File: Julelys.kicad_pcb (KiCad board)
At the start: 4 copper layers, 65 x 56 mm, 124 parts, among them J1 Raspberry_Pi_40pin, J10 B3B-XH-A, J11 B3B-XH-A, J12 Conn_01x03_Pin, J13 FAN, J3 Conn_02x06_Odd_Even, J4 B3B-XH-A, J5 B3B-XH-A, J6 B3B-XH-A, J7 B3B-XH-A, J8 B3B-XH-A, J9 B3B-XH-A, P1 USB_C_Receptacle_USB2.0, Q1 AO3400A, SW1 SW_Push, SW2 SW_Push, U1 ESP32-C3-WROOM-02, U10 74LVC1G08, U2 74HC4051, U3 AMS1117-3.3, U4 BC847BDW1T1G, U5 CP2102N-A02-GQFN28, U6 74AHCT1G125, U7 74AHCT1G125, U8 74AHCT1G125, U9 74AHCT1G125

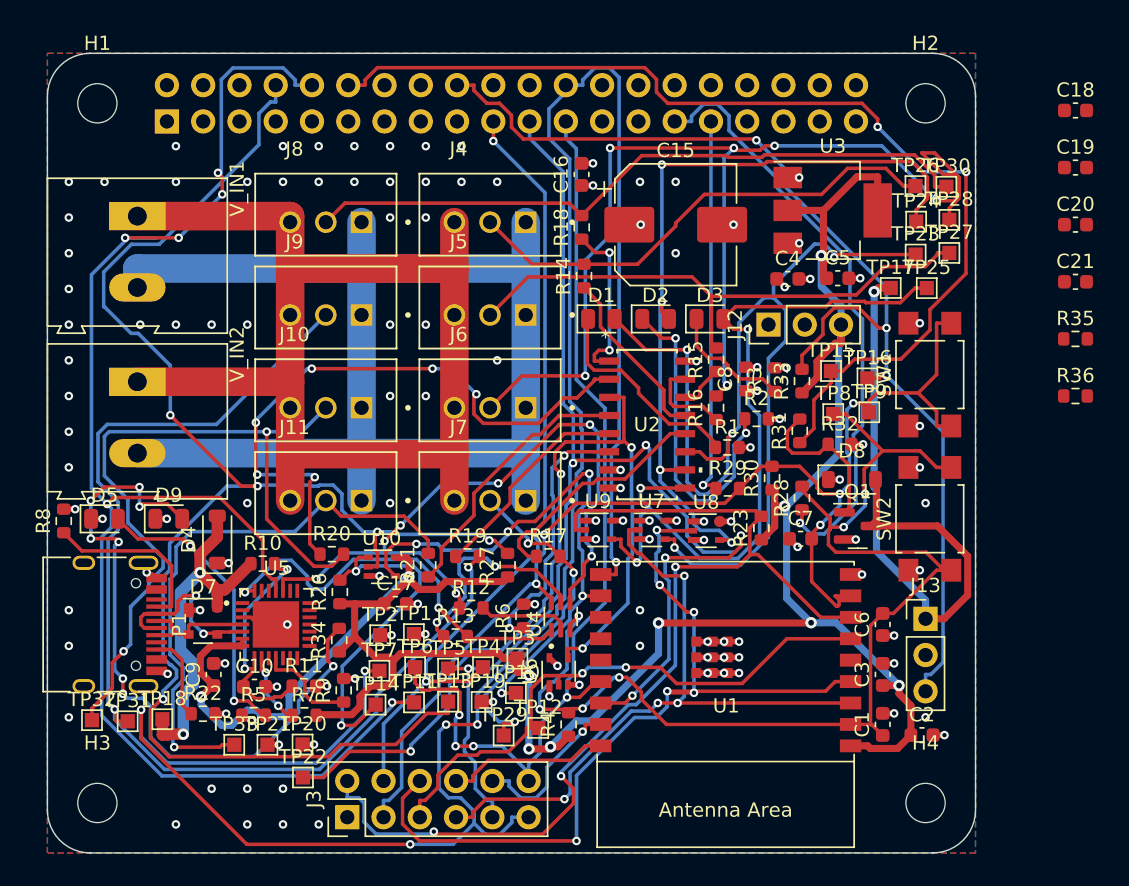
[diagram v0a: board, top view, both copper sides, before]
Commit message: Place decoupling caps, remove fan circuit and J3, add spare ESP32-Pi lines
Schematic:
- Remove the fan circuit (J13, Q1, D8, R31-R33, TP15-17); the Pi 5 drives
  its own Active Cooler. J1 pins 12/18 are now no-connect
- Remove the J3 debug header; J1 doubles as the dev header without a Pi
- IO0/IO1 to J1 pins 37/36 (Pi GPIO26/16) through R37/R38 1k as spare lines

Board:
- Test points moved to the bottom side to free space on top
- Decoupling caps C2/C3/C5/C8/C16/C18-C21 and R35/R36 placed next to
  their ICs; U8 nudged and R23/R10 moved to make room
- Conflicting tracks ripped up and rerouted; 6 connections left for
  interactive routing
- Back pinout table updated (fan and J3 rows replaced by J1 37/36)
- Courtyard exception rule for caps inside their IC's courtyard margin
- DRC (JLCPCB rules): 0 errors; ERC: 0 errors; schematic parity clean

Co-Authored-By: Claude Opus 5.5 <noreply@anthropic.com>
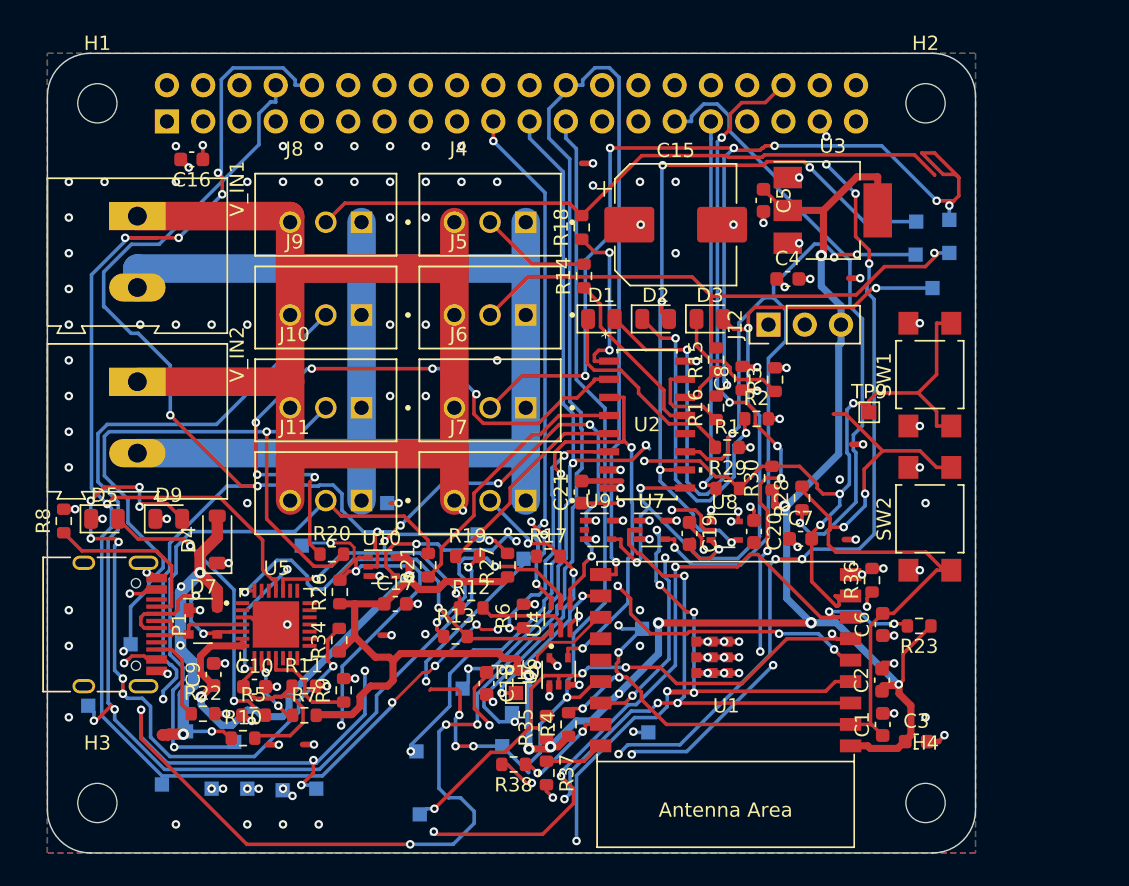
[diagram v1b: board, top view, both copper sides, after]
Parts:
- removed D8: 1N5819HW-7-F, Diode_SMD:D_SOD-123
- removed J13: FAN, Connector_PinHeader_2.54mm:PinHeader_1x03_P2.54mm_Vertical
- removed J3: Conn_02x06_Odd_Even, Connector_PinHeader_2.54mm:PinHeader_2x06_P2.54mm_Vertical
- removed Q1: AO3400A, Package_TO_SOT_SMD:SOT-23
- removed R31: 100, Resistor_SMD:R_0603_1608Metric
- removed R32: 100K, Resistor_SMD:R_0603_1608Metric
- removed R33: 10K, Resistor_SMD:R_0603_1608Metric
- removed TP15: FAN_PWM, TestPoint:TestPoint_Pad_1.0x1.0mm
- removed TP16: FAN_TACH, TestPoint:TestPoint_Pad_1.0x1.0mm
- removed TP17: FAN_N, TestPoint:TestPoint_Pad_1.0x1.0mm
- added R37: 1K, R_0603_1608Metric, F.Cu at (55.0, 62.4)
- added R38: 1K, R_0603_1608Metric, F.Cu at (52.6, 61.8)
- TP1, TP11, TP12, TP13, TP14, TP18, TP19, TP2, TP20, TP21, TP22, TP23, TP24, TP25, TP26, TP27, TP28, TP29, TP3, TP30, TP31, TP32, TP33, TP4, TP5, TP6, TP7, TP8: moved to B.Cu
- moved C18 57.5 mm to (50.8, 56.1), turned to -90 degrees
- moved R35 46.0 mm to (55.0, 59.2), turned to 90 degrees
- moved TP30 43.5 mm to (39.5, 23.8), turned to 180 degrees
- moved C21 37.6 mm to (57.4, 42.7), turned to 90 degrees
- moved C19 37.2 mm to (65.0, 45.6), turned to -90 degrees
- moved C20 31.1 mm to (69.5, 45.5), turned to -90 degrees
- moved TP26 29.9 mm to (51.0, 23.8), turned to 180 degrees
- moved C16 27.3 mm to (30.1, 19.4), turned to 180 degrees
- moved TP8 20.1 mm to (61.6, 52.3), turned to 180 degrees
- moved R36 19.2 mm to (77.8, 48.9), turned to 90 degrees
- moved TP11 18.6 mm to (28.0, 63.2), turned to 180 degrees
- moved TP19 15.2 mm to (36.5, 63.6), turned to 180 degrees
- moved R23 13.0 mm to (81.0, 52.1), turned to 180 degrees
- moved R10 12.3 mm to (33.7, 60.0)
- moved TP14 12.3 mm to (37.8, 46.5), turned to 180 degrees
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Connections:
- J1 pad 12: FAN_PWM -> unconnected-(J1-Pin_12-Pad12)
- J1 pad 18: FAN_TACH -> unconnected-(J1-Pin_18-Pad18)
- J1 pad 36: unconnected-(J1-Pin_36-Pad36) -> PI_GPIO16
- J1 pad 37: unconnected-(J1-Pin_37-Pad37) -> PI_GPIO26
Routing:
- net FAN_TACH: track 78.9 -> 0.00 mm, vias 3 -> 0
- net FAN_PWM: track 74.0 -> 0.00 mm, vias 2 -> 0
- net PI_GPIO16: track 0.00 -> 71.5 mm, vias 0 -> 9
- net PI_GPIO26: track 0.00 -> 65.5 mm, vias 0 -> 8
- net /Power/FAN_N: track 43.1 -> 0.00 mm, vias 1 -> 0
- net IO2: track 94.6 -> 64.5 mm, vias 6 -> 5
- net /CH1: track 34.4 -> 7.80 mm
- net PI_TX: track 109.7 -> 83.2 mm
- net A2: track 72.9 -> 53.6 mm, vias 3 -> 5
- net TXD: track 105.8 -> 124.0 mm, vias 6 -> 10
- net IO9: track 84.6 -> 66.8 mm, vias 5 -> 7
- net /MCH4: track 16.7 -> 0.00 mm
- net GND: track 147.3 -> 163.6 mm, vias 115 -> 121
- net IO6: track 56.9 -> 72.8 mm, vias 2 -> 6
- net VBUS: track 25.6 -> 38.4 mm, vias 2 -> 7
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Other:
- board text added: "IO0 / IO1 (1k)"
- board text added: "J1 37/36"
- board text removed: "1 FAN- 2 +5V 3 TACH"
- board text removed: "1 GND 2 IO8 3 IO9"
- board text removed: "10 IO1 11 IO10 12 IO3"
- board text removed: "4 IO6 5 IO7 6 IO5"
- board text removed: "7 IO4 8 IO0 9 IO2"
- board text removed: "J13 FAN"
- board text removed: "J3"

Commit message: Re-layout v4 with ESP32 under the GPIO header, board fully routed
- ESP32 (U1) top-right under J1, antenna at the right edge (used only as a
  standalone dev board; on the Pi the link is SPI). Short SPI/UART/EN/BOOT
  and spare lines to J1
- Mux U2 with level shifters, series resistors and D1-D3 bottom-centre;
  regulator U3 and Pi bulk cap C15 bottom-left next to the CP2102N
- All decoupling caps 1.7-3.2 mm from their IC pins (C16 5 mm from J1)
- R5 moved next to D5 to free the U5 pin escape; buttons moved under
  the antenna area on the right edge
- Routed with Freerouting plus scripted cleanup; keep-outs now read from
  the board's rule areas
- DRC (JLCPCB rules): 0 errors, 0 unconnected; ERC 0 errors; parity clean

Co-Authored-By: Claude Opus 5.5 <noreply@anthropic.com>
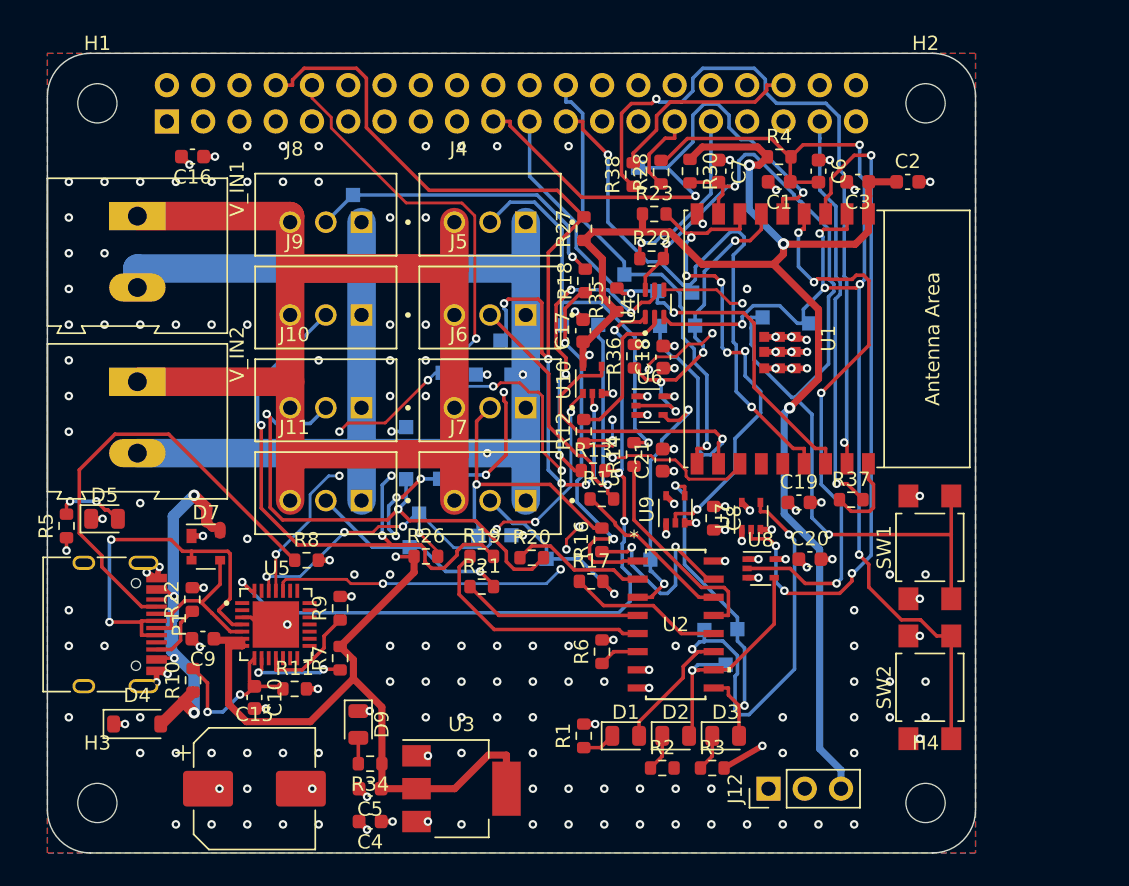
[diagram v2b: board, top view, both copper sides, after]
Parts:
- TP10, TP9: moved to B.Cu
- moved C5 49.6 mm to (42.6, 63.5), turned to 180 degrees
- moved C15 49.3 mm to (34.5, 63.5)
- moved U3 48.1 mm to (49.0, 63.5)
- moved C4 48.0 mm to (42.6, 65.8), turned to 180 degrees
- moved R4 42.4 mm to (71.2, 19.2), turned to 0 degrees
- moved R38 42.2 mm to (61.0, 20.5), turned to 90 degrees
- moved TP7 42.0 mm to (60.4, 27.5)
- moved TP28 39.7 mm to (50.2, 45.8)
- moved C3 39.4 mm to (76.8, 21.0), turned to 180 degrees
- moved TP12 39.3 mm to (65.4, 31.1)
- moved C1 38.7 mm to (71.2, 21.0), turned to 180 degrees
- moved C2 34.9 mm to (80.2, 21.0), turned to 0 degrees
- moved TP11 34.9 mm to (47.7, 34.4)
- moved TP6 34.4 mm to (65.2, 28.8)
- moved R23 34.3 mm to (62.5, 23.2), turned to 0 degrees
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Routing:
- net CS: track 156.8 -> 32.9 mm, vias 8 -> 1
- net /CH3: track 78.0 -> 19.6 mm, vias 7 -> 1
- net PI_GPIO16: track 71.5 -> 14.0 mm, vias 9 -> 0
- net /Power/LED_3V3: track 48.4 -> 1.81 mm, vias 8 -> 0
- net TXD: track 124.0 -> 78.5 mm, vias 10 -> 8
- net IO1: track 7.12 -> 49.3 mm
- net /AS0: track 77.3 -> 36.2 mm, vias 5 -> 2
- net PI_GPIO26: track 65.5 -> 28.5 mm, vias 8 -> 1
- net PI_EN: track 42.3 -> 5.85 mm, vias 1 -> 0
- net /Data: track 53.8 -> 18.4 mm, vias 4 -> 2
- net /AS1: track 52.7 -> 17.5 mm, vias 5 -> 1
- net /MCH7: track 44.0 -> 9.55 mm, vias 6 -> 0
- net IO6: track 72.8 -> 39.7 mm, vias 6 -> 2
- net /CH6: track 80.0 -> 47.0 mm, vias 3 -> 4
- net /AS2: track 53.4 -> 23.8 mm, vias 4 -> 2
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
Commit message: Test board layout: bare ESP32-C3 placed and mostly routed (WIP)
- Board synced to the new schematic: CP2102N/U4/U10 removed; ESP32-C3FH4,
  crystal, RF match, Walsin antenna, TVS, pull-downs and new caps added
- Project footprint library Julelys.pretty with the Walsin RFANT3216120A5T
  land pattern and a 6x6 mm antenna keep-out (no pour, feed track allowed)
- Stackup set to JLC04161H-7628 (0.21 mm prepreg); RF (0.33 mm) and USB
  net classes; In2.Cu is a mixed layer (signals + +5V pour)
- Zones join SMD pads solid; J1 solid to the planes
- DRC: 0 errors; 14 QFN fan-out connections left for interactive routing
  (listed in docs/esp32-c3-chip-design.md)

Co-Authored-By: Claude Opus 5.5 <noreply@anthropic.com>
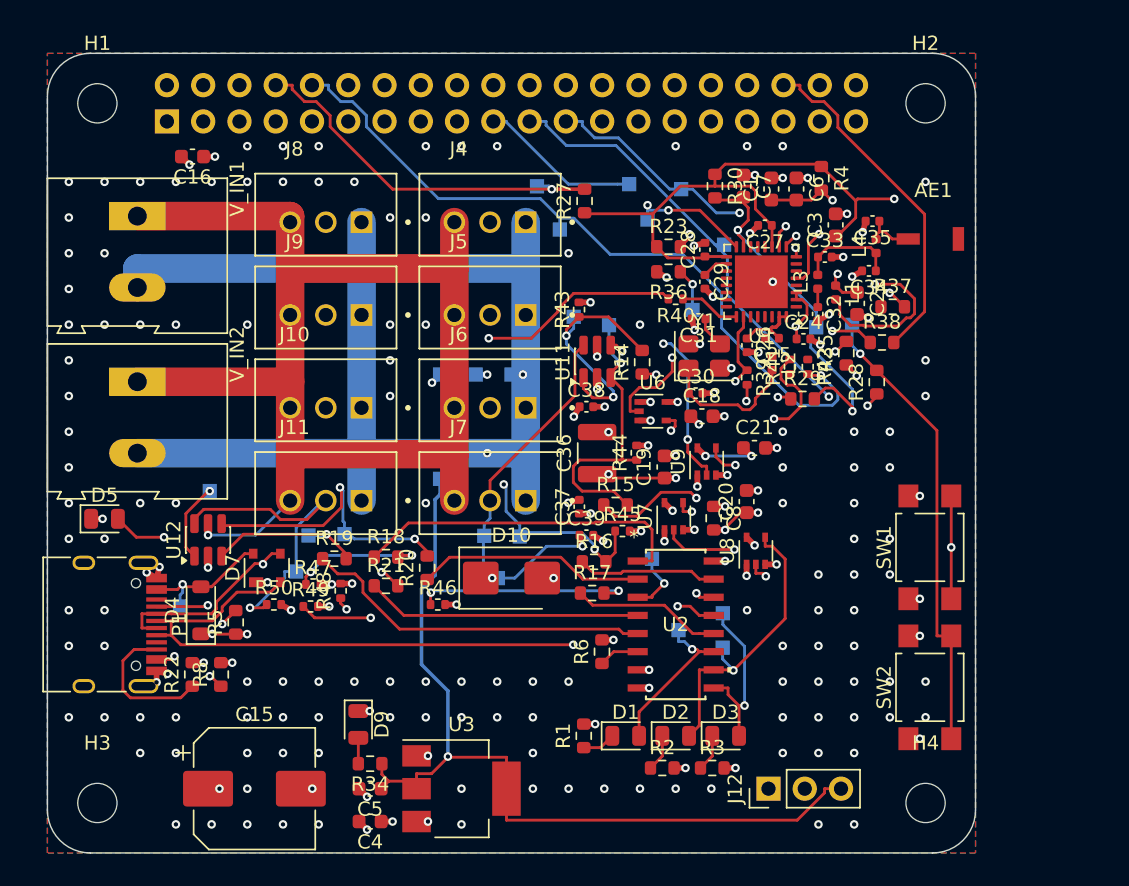
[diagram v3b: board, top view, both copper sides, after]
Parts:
- removed C10: 1uF/16V(10%), Capacitor_SMD:C_0603_1608Metric
- removed C17: 100nF, Capacitor_SMD:C_0603_1608Metric
- removed C9: 10uF/25V(20%), Capacitor_SMD:C_0603_1608Metric
- removed R10: 22.1K, Resistor_SMD:R_0603_1608Metric
- removed R11: 47.5K, Resistor_SMD:R_0603_1608Metric
- removed R12, R13: 10k, Resistor_SMD:R_0603_1608Metric
- removed R26, R9: 10K, Resistor_SMD:R_0603_1608Metric
- removed R7: 1K, Resistor_SMD:R_0603_1608Metric
- removed TP13: PI_TX, TestPoint:TestPoint_Pad_1.0x1.0mm
- removed TP14: USB_TX, TestPoint:TestPoint_Pad_1.0x1.0mm
- removed U10: 74LVC1G08, Package_TO_SOT_SMD:SOT-353_SC-70-5
- removed U4: BC847BDW1T1G, Transistor_Power_Module:SOT65P210X110-6N
- removed U5: CP2102N-A02-GQFN28, Connector_USB:QFN50P500X500X80-29N
- added AE1: RFANT3216120A5T, Julelys:Walsin_RFANT3216120A5T, F.Cu at (80.3, 25.0)
- added C24: 1uF, Capacitor_SMD:C_0402_1005Metric, F.Cu at (73.0, 32.0)
- added C25: 1uF, Capacitor_SMD:C_0402_1005Metric, F.Cu at (70.8, 31.9)
- added C26: 10nF, Capacitor_SMD:C_0402_1005Metric, F.Cu at (69.0, 32.5)
- added C27: 100nF, Capacitor_SMD:C_0402_1005Metric, F.Cu at (70.2, 24.1)
- added C28: 100nF, Capacitor_SMD:C_0402_1005Metric, F.Cu at (66.0, 25.8)
- added C29: 1uF, Capacitor_SMD:C_0402_1005Metric, F.Cu at (66.0, 28.0)
- added C30: 22pF, Capacitor_SMD:C_0402_1005Metric, F.Cu at (65.4, 35.8)
- added C31: 22pF, Capacitor_SMD:C_0402_1005Metric, F.Cu at (65.6, 30.6)
- added C32: 1.5pF, Capacitor_SMD:C_0402_1005Metric, F.Cu at (74.0, 30.2)
- added C33: 1.5pF, Capacitor_SMD:C_0402_1005Metric, F.Cu at (74.5, 26.3)
- added C34: DNP, Capacitor_SMD:C_0402_1005Metric, F.Cu at (77.5, 27.2)
- added C35: DNP, Capacitor_SMD:C_0402_1005Metric, F.Cu at (77.8, 23.8)
- added C36: 100uF, Capacitor_SMD:C_1210_3225Metric, F.Cu at (58.5, 40.0)
- added C37: 100nF, Capacitor_SMD:C_0402_1005Metric, F.Cu at (57.2, 43.8)
- added C38: 100nF, Capacitor_SMD:C_0402_1005Metric, F.Cu at (57.8, 36.8)
- added C39: 100nF, Capacitor_SMD:C_0402_1005Metric, F.Cu at (57.8, 45.8)
- added D10: SMBJ5.0A, Diode_SMD:D_SMB, F.Cu at (52.5, 48.8)
- added L1: 2.0nH, Inductor_SMD:L_0402_1005Metric, F.Cu at (75.2, 28.8)
- added L2: 24nH, Inductor_SMD:L_0402_1005Metric, F.Cu at (70.8, 33.7)
- added L3: 2.7nH, Inductor_SMD:L_0402_1005Metric, F.Cu at (74.0, 28.0)
- added L4: 6.8nH, Inductor_SMD:L_0402_1005Metric, F.Cu at (78.0, 25.5)
- added R39: 22, Resistor_SMD:R_0402_1005Metric, F.Cu at (69.0, 34.7)
- added R40: 22, Resistor_SMD:R_0402_1005Metric, F.Cu at (64.0, 29.2)
- added R41: 1.5K, Resistor_SMD:R_0402_1005Metric, F.Cu at (72.0, 34.0)
- added R42: 499, Resistor_SMD:R_0402_1005Metric, F.Cu at (73.2, 34.0)
- added R43: 10K, Resistor_SMD:R_0402_1005Metric, F.Cu at (57.2, 29.9)
- added R44: 10K, Resistor_SMD:R_0402_1005Metric, F.Cu at (61.3, 40.0)
- added R45: 10K, Resistor_SMD:R_0402_1005Metric, F.Cu at (60.3, 45.5)
- added R46: 10K, Resistor_SMD:R_0402_1005Metric, F.Cu at (47.3, 50.6)
- added R47: 10K, Resistor_SMD:R_0402_1005Metric, F.Cu at (38.6, 49.2)
- added R48: 10K, Resistor_SMD:R_0402_1005Metric, F.Cu at (40.5, 49.6)
- added R49: 10K, Resistor_SMD:R_0402_1005Metric, F.Cu at (38.4, 50.7)
- added R50: 10K, Resistor_SMD:R_0402_1005Metric, F.Cu at (35.9, 50.6)
- added U11: SRV05-4, Package_TO_SOT_SMD:SOT-23-6, F.Cu at (58.5, 33.6)
- added U12: SRV05-4, Package_TO_SOT_SMD:SOT-23-6, F.Cu at (31.2, 46.1)
- added Y1: 40MHz, Crystal:Crystal_SMD_3225-4Pin_3.2x2.5mm, F.Cu at (66.0, 33.2)
- C18, C19, C20, C21: footprint C_0603_1608Metric -> Capacitor_SMD:C_0603_1608Metric
- R35, R36, R37, R38: footprint R_0603_1608Metric -> Resistor_SMD:R_0603_1608Metric
- U1: value ESP32-C3-WROOM-02 -> ESP32-C3FH4; footprint PCM_Espressif:ESP32-C3-WROOM-02 -> Package_DFN_QFN:QFN-32-1EP_5x5mm_P0.5mm_EP3.7x3.7mm
- moved R18 23.9 mm to (43.7, 47.3), turned to 0 degrees
- moved TP30 23.0 mm to (31.4, 42.7)
- moved R28 21.1 mm to (78.1, 35.0)
- moved R38 21.0 mm to (78.5, 32.2), turned to 0 degrees
- moved R35 16.5 mm to (76.0, 33.0)
- moved R29 14.4 mm to (72.9, 36.2)
- moved R37 13.8 mm to (79.2, 29.8)
- moved R5 13.6 mm to (33.2, 51.9)
- moved TP10 13.0 mm to (54.3, 21.3)
- moved TP11 13.0 mm to (55.9, 24.3)
- moved TP21 12.3 mm to (47.5, 34.5)
- moved TP1 12.3 mm to (51.5, 48.8)
- moved R19 10.3 mm to (40.1, 47.4)
- moved TP31 10.2 mm to (38.3, 45.8)
- moved R8 10.0 mm to (32.1, 55.5), turned to 90 degrees
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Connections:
- D7 pad 2: Net-(U5-D+) -> USB_D+
- D7 pad 3: Net-(U5-D-) -> USB_D-
- J1 pad 8: PI_TX -> RXD
- P1 pad A6: Net-(U5-D+) -> USB_D+
- P1 pad A7: Net-(U5-D-) -> USB_D-
- P1 pad B6: Net-(U5-D+) -> USB_D+
- P1 pad B7: Net-(U5-D-) -> USB_D-
- R27 pad 2: PI_TX -> RXD
- U1 pad 1: +3.3V -> /ESP32/RF_IN
- U1 pad 10: CS -> A1
- U1 pad 11: RXD -> +3.3V
- U1 pad 12: TXD -> IO6
- U1 pad 13: USB_D- -> IO7
- U1 pad 14: USB_D+ -> A2
- U1 pad 15: CLK -> IO9
- U1 pad 16: IO2 -> CS
- U1 pad 17: IO1 -> +3.3V
- U1 pad 18: IO0 -> /ESP32/VDD_SPI
- U1 pad 19: GND -> unconnected-(U1-SPIHD-Pad19)
- U1 pad 2: CHIP_UP -> /ESP32/VDD3P3
- U1 pad 3: A0 -> /ESP32/VDD3P3
- U1 pad 4: A1 -> IO0
- U1 pad 5: IO6 -> IO1
- U1 pad 6: IO7 -> IO2
- U1 pad 7: A2 -> CHIP_UP
- U1 pad 8: IO9 -> CLK
- U1 pad 9: GND -> A0
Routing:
- net +5V: track 96.7 -> 217.9 mm, vias 16 -> 26
- net USB_D+: track 0.00 -> 72.3 mm, vias 0 -> 2
- net PI_TX: track 67.4 -> 0.00 mm, vias 5 -> 0
- net USB_D-: track 0.00 -> 59.3 mm, vias 0 -> 2
- net RTS: track 57.6 -> 0.00 mm, vias 9 -> 0
- net DTR: track 52.8 -> 0.00 mm, vias 4 -> 0
- net /ESP32/VDD3P3: track 0.00 -> 41.4 mm, vias 0 -> 2
- net CHIP_UP: track 89.6 -> 49.1 mm, vias 6 -> 2
- net USB_TX: track 37.7 -> 0.00 mm, vias 7 -> 0
- net A1: track 39.7 -> 3.04 mm, vias 4 -> 2
- net IO1: track 49.3 -> 14.2 mm
- net PI_EN: track 5.85 -> 36.8 mm, vias 0 -> 1
- net IO6: track 39.7 -> 11.4 mm, vias 2 -> 0
- net IO9: track 73.5 -> 45.9 mm
- net Net-(U5-D+): track 26.9 -> 0.00 mm, vias 2 -> 0
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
